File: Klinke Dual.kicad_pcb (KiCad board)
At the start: 2 copper layers, 30 x 30 mm, 9 parts, among them J1 AudioJack3_Dual_Ground_Switch, J2 Conn_01x03, J3 Conn_01x03

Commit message: Update to latest files
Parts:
- removed H4: MountingHole_Pad, MountingHole:MountingHole_3.2mm_M3_DIN965_Pad
- H3: value MountingHole_Pad -> MountingHole; footprint MountingHole:MountingHole_3.2mm_M3_DIN965_Pad -> MountingHole:MountingHole_3.2mm_M3_DIN965
- moved J3 21.0 mm to (143.0, 88.6), turned to 90 degrees
- moved JP1 17.3 mm to (150.0, 81.5), turned to 180 degrees
- moved J2 16.5 mm to (151.9, 88.6), turned to 90 degrees
- moved JP2 15.5 mm to (150.0, 84.2), turned to 180 degrees
- moved H3 11.0 mm to (150.0, 111.0)
- moved H1 7.81 mm to (145.0, 84.0)
- moved H2 7.81 mm to (155.0, 84.0)
- moved J1 0.50 mm to (157.0, 94.5)
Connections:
- H3 pad 1: Earth -> (no net)
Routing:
- net /LEFT1: track 29.2 -> 7.88 mm
- net /RIGHT1: track 36.9 -> 17.4 mm
- net /GND2: track 18.4 -> 0.00 mm
- net /RIGHT2: track 7.18 -> 22.0 mm
- net /LEFT2: track 6.72 -> 19.9 mm
- net Earth: track 4.76 -> 0.85 mm, vias 0 -> 1
- net /GND1: track 2.46 -> 0.00 mm
- added copper zone on B.Cu, net /GND1
- added copper zone on B.Cu, net /GND2
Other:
- board size 30 x 30 mm -> 18 x 35 mm
- board text added: "Dual Klinke Rev. 2, 2021-03-13 Tobias Müller, twam.info"
- board text added: "GLRGLR"
- board text removed: "Dual Klinke Rev. 1, 2021-03-06 Tobias Müller, twam.info"
- board text removed: "G"
- board text removed: "L"
- board text removed: "R"

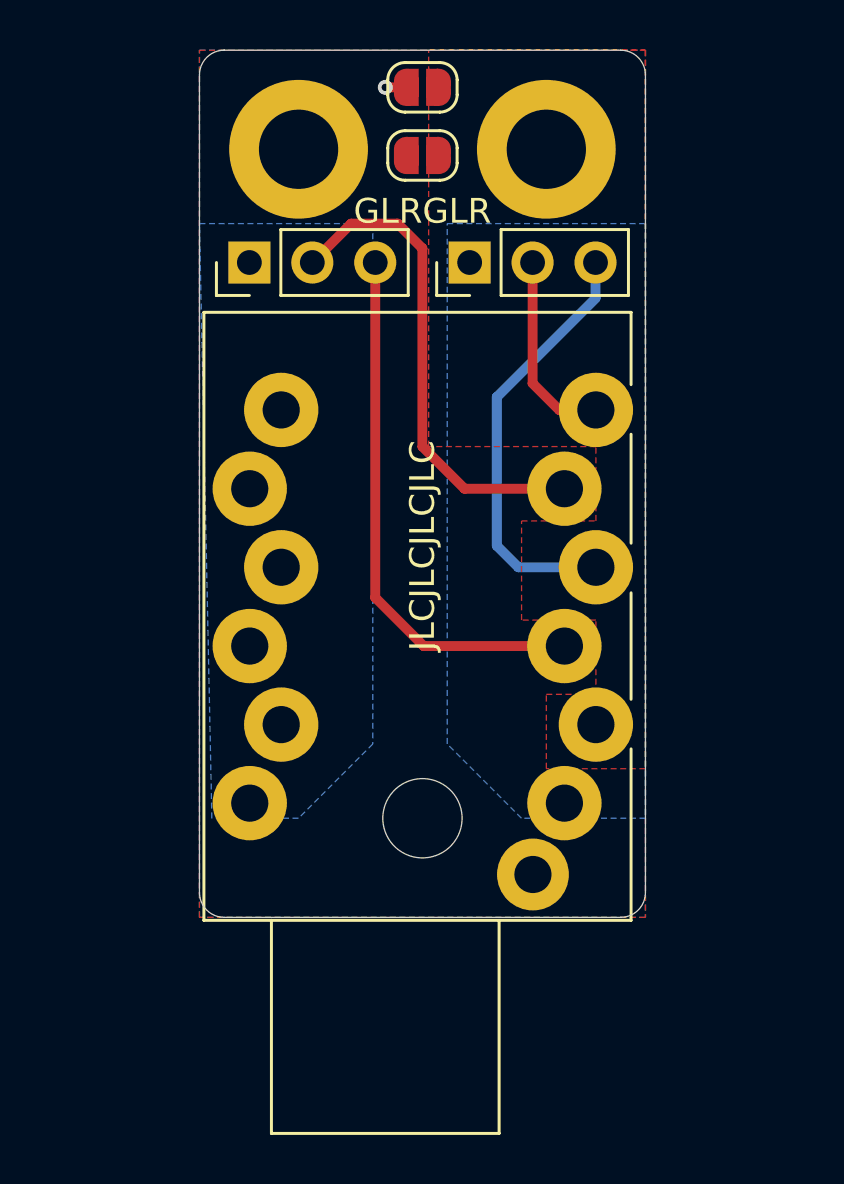
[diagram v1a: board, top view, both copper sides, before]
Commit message: Update to KiCad 6
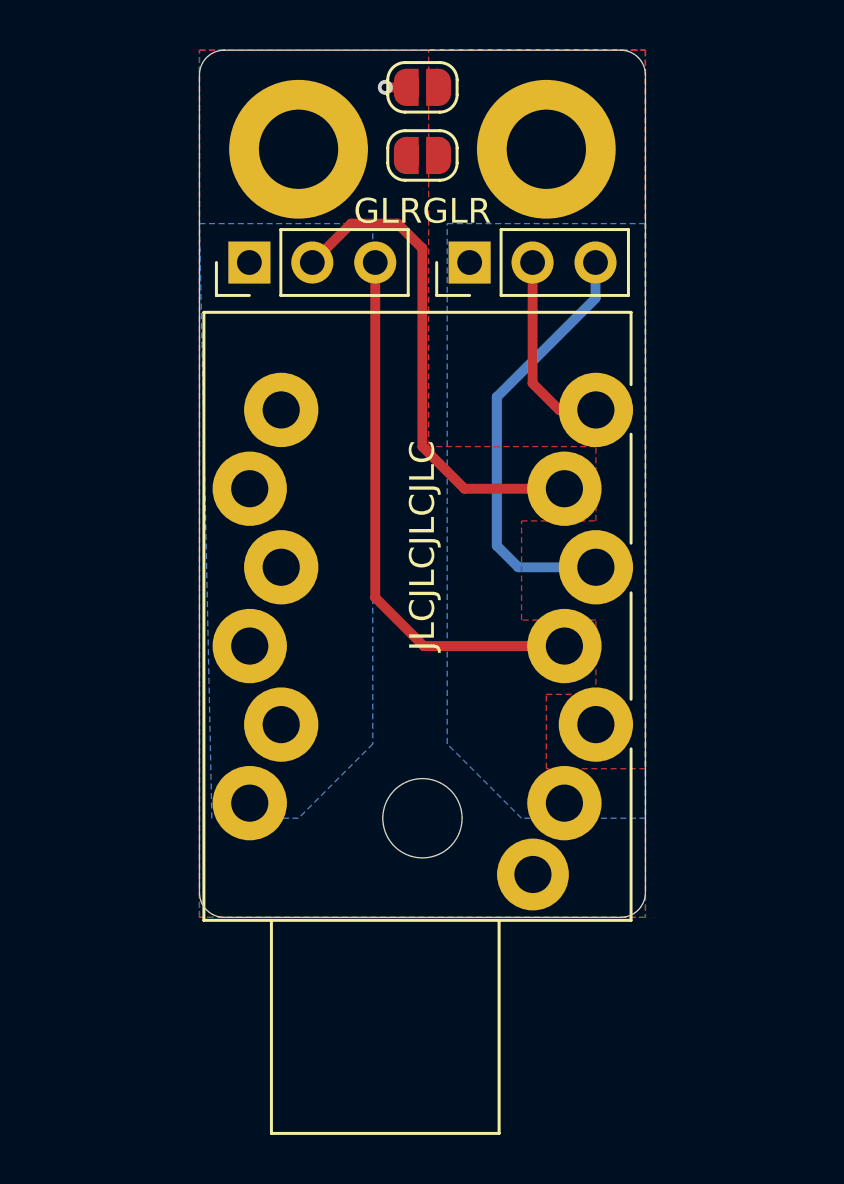
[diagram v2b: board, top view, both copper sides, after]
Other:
- net class Default removed
